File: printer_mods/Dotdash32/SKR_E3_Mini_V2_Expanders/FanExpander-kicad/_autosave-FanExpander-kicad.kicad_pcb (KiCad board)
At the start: 2 copper layers, 62.2 x 21.3 mm, 65 parts, among them J0 FAN0, J1 FAN1, J10 FAN0_IN, J11 HI_PWR_IN, J2 FAN2, J3 FAN3, J4 FAN4, J5 FAN5, J6 FAN6, J7 FAN7, J8 EXP1_IN, J9 5V_In, Q1 IRLML6344, Q2 IRLML6344, Q3 IRLML6344, Q4 IRLML6344, Q5 IRLML6344, Q6 IRLML6344, Q7 IRLML6344

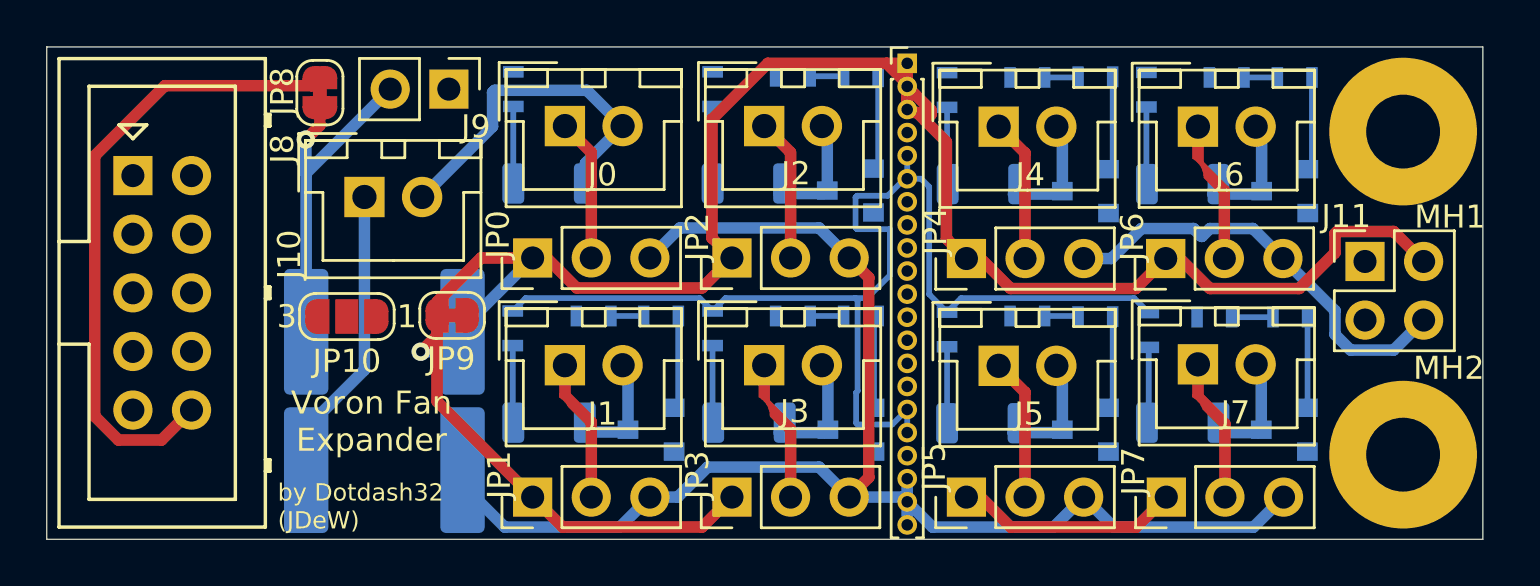
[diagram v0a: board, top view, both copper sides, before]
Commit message: chore: trying routing, running into obstacles
no room to route the control wires, everything else is *almost*
there though.
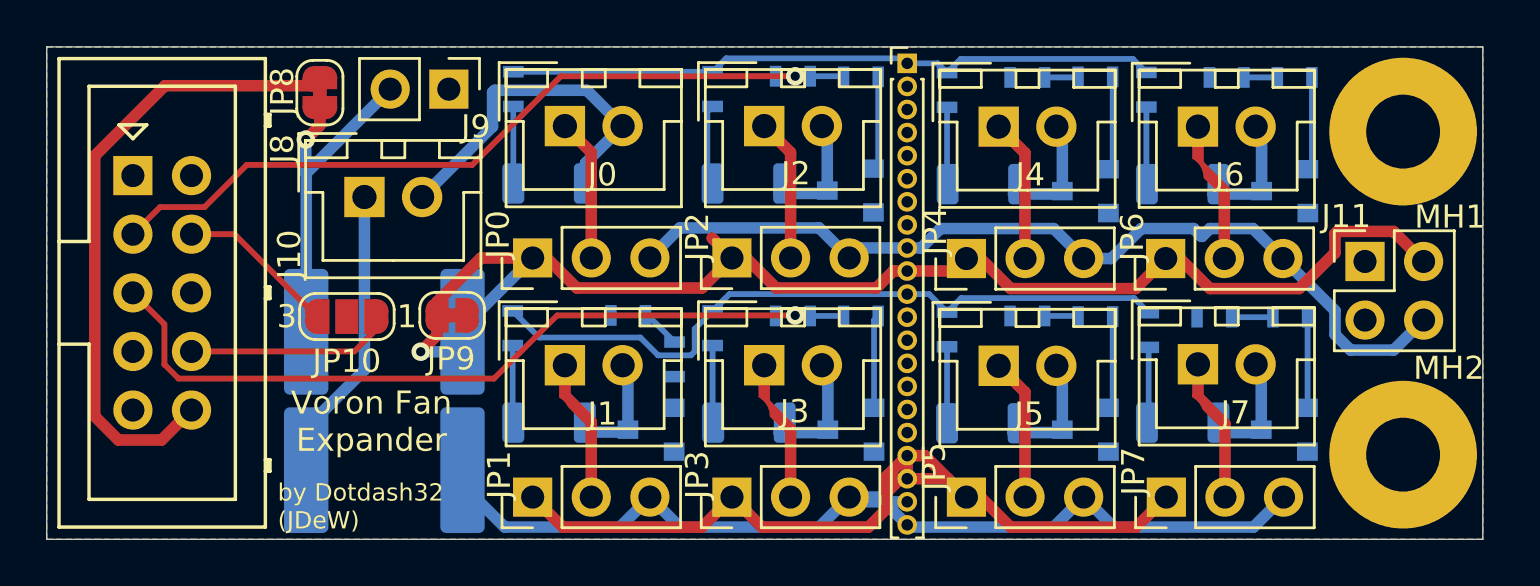
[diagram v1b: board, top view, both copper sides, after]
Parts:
- moved R5 1.97 mm to (66.8, 53.6), turned to 90 degrees
- moved R9 1.50 mm to (64.8, 51.7)
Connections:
- SPL1 pad 1: +5V -> /LED_Drive
- SPL1 pad 10: GND -> +5V
- SPL1 pad 11: GND -> /LED_Drive
- SPL1 pad 12: GND -> Net-(SPL1-Pad12)
- SPL1 pad 13: GND -> Net-(SPL1-Pad13)
- SPL1 pad 14: /FAN7 -> Net-(SPL1-Pad14)
- SPL1 pad 15: /FAN5 -> Net-(SPL1-Pad15)
- SPL1 pad 16: /LED_Drive -> Net-(SPL1-Pad16)
- SPL1 pad 17: /LED_Drive -> Net-(SPL1-Pad17)
- SPL1 pad 18: GND -> +5V
- SPL1 pad 19: +24V -> +5V
- SPL1 pad 2: +5V -> Net-(SPL1-Pad2)
- SPL1 pad 3: +5V -> Net-(SPL1-Pad3)
- SPL1 pad 4: GND -> Net-(SPL1-Pad4)
- SPL1 pad 5: /LED_Drive -> Net-(SPL1-Pad5)
- SPL1 pad 6: /LED_Drive -> Net-(SPL1-Pad6)
- SPL1 pad 7: /FAN4 -> Net-(SPL1-Pad7)
- SPL1 pad 8: /FAN6 -> Net-(SPL1-Pad8)
- SPL1 pad 9: GND -> +24V
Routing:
- net /FAN3: track 1.45 -> 34.5 mm, vias 0 -> 1
- net /FAN2: track 1.46 -> 33.6 mm, vias 0 -> 1
- net /LED_Drive: track 50.9 -> 60.1 mm
- net Net-(J8-Pad8): track 0.00 -> 8.97 mm
- net +5V: track 106.2 -> 97.7 mm
- net Net-(J8-Pad4): track 0.00 -> 6.91 mm
- net Net-(Q1-Pad1): track 4.05 -> 0.26 mm
- net +24V: track 82.4 -> 83.2 mm
- added copper zone on B.Cu, net GND
- added copper zone on F.Cu, net GND
